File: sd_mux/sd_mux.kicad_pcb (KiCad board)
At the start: 2 copper layers, 86.4 x 54.6 mm, 22 parts, among them IC1 SN74CBT3257DR, IC2 SN74CBT3257DR, J1 MICRO SD CARD, J2 DEVICE 1, J3 DEVICE 2, J4 CONTROL

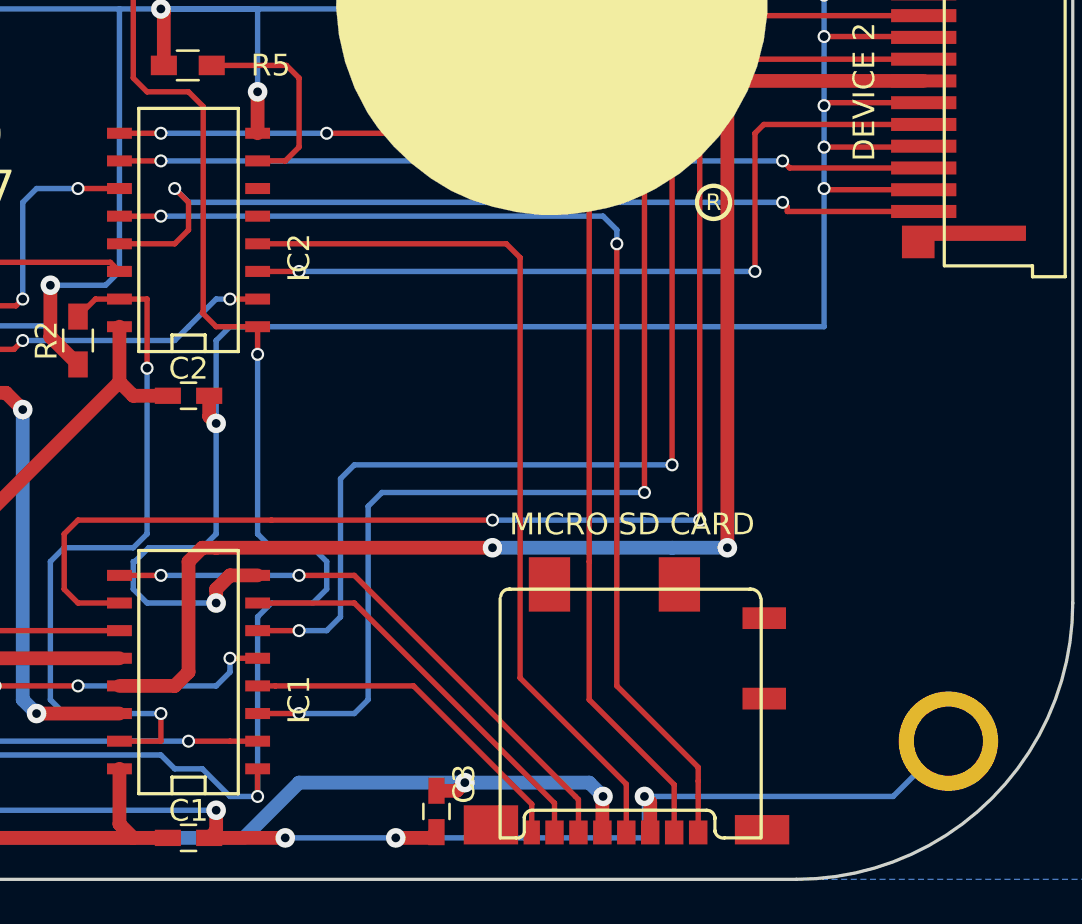
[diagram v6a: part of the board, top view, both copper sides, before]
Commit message: swapped SD card footprint
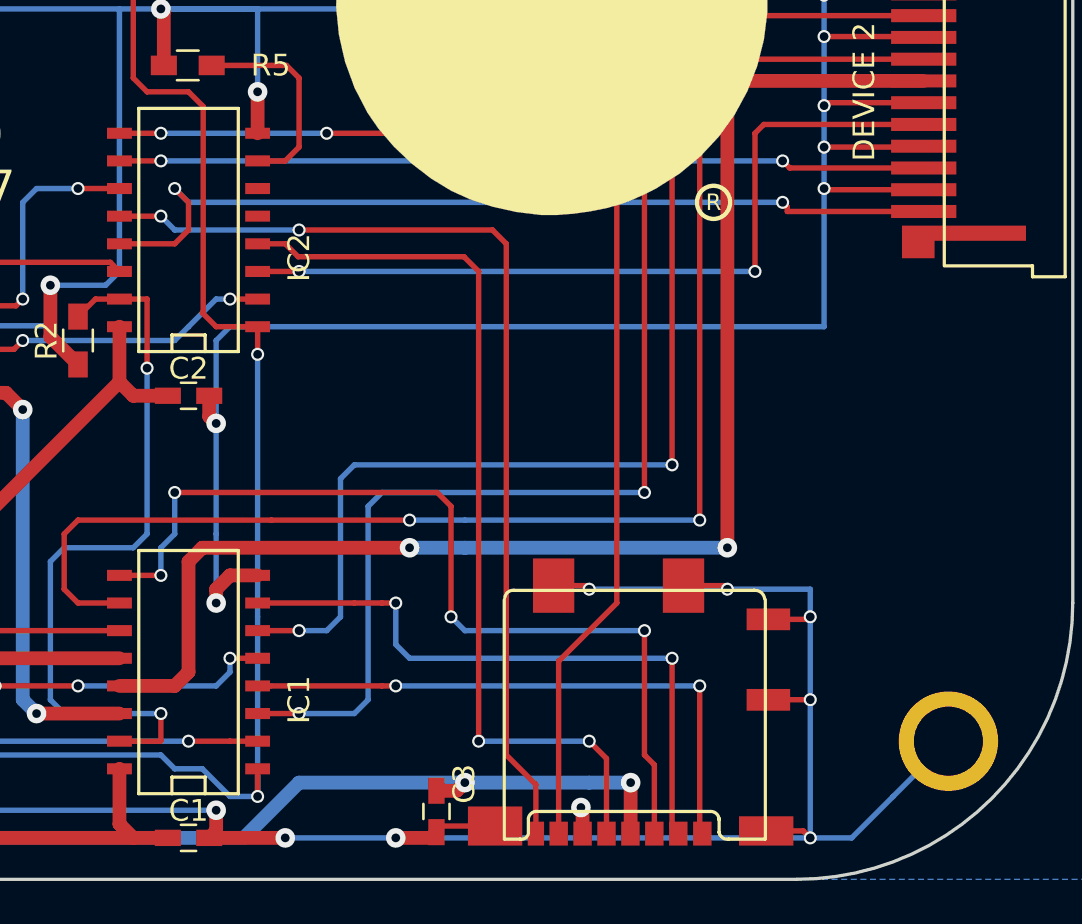
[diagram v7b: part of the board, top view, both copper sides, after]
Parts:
- J1: value MICRO SD CARD -> Micro_SD_Card_Det
- moved J1 0.20 mm to (167.8, 120.1)
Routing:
- net GND: track 364.7 -> 392.1 mm, vias 21 -> 26
- net Net-(IC1-Pad9): track 26.9 -> 42.7 mm, vias 2 -> 4
- net Net-(IC1-Pad4): track 16.2 -> 27.2 mm, vias 0 -> 2
- net Net-(IC1-Pad7): track 18.8 -> 29.4 mm, vias 0 -> 2
- net Net-(IC2-Pad12): track 52.4 -> 46.0 mm
- net device_select: track 107.7 -> 103.4 mm
- net Net-(C3-Pad1): track 50.7 -> 52.4 mm
- net Net-(IC2-Pad4): track 40.8 -> 41.9 mm, vias 0 -> 2
- net Net-(IC2-Pad9): track 55.0 -> 55.8 mm

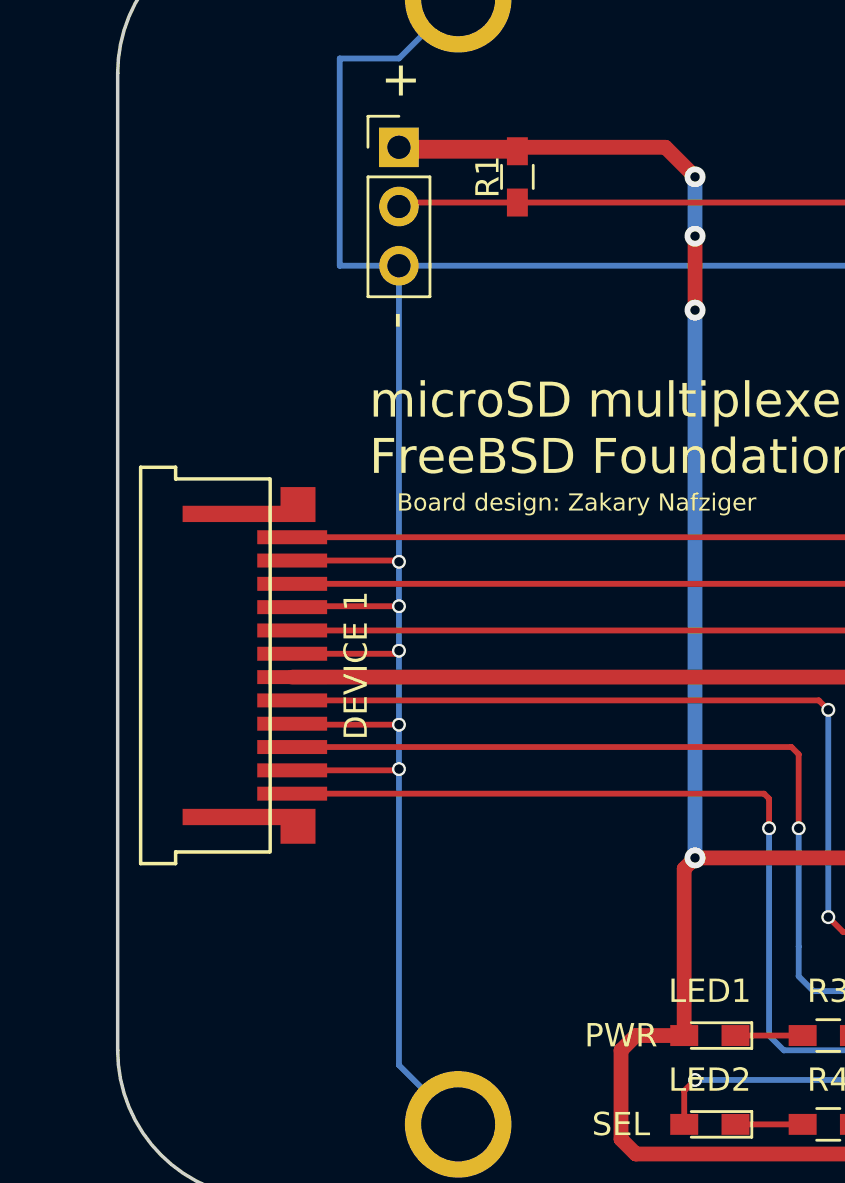
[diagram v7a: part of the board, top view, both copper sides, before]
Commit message: rerouted power line to avoid cut in ground plane
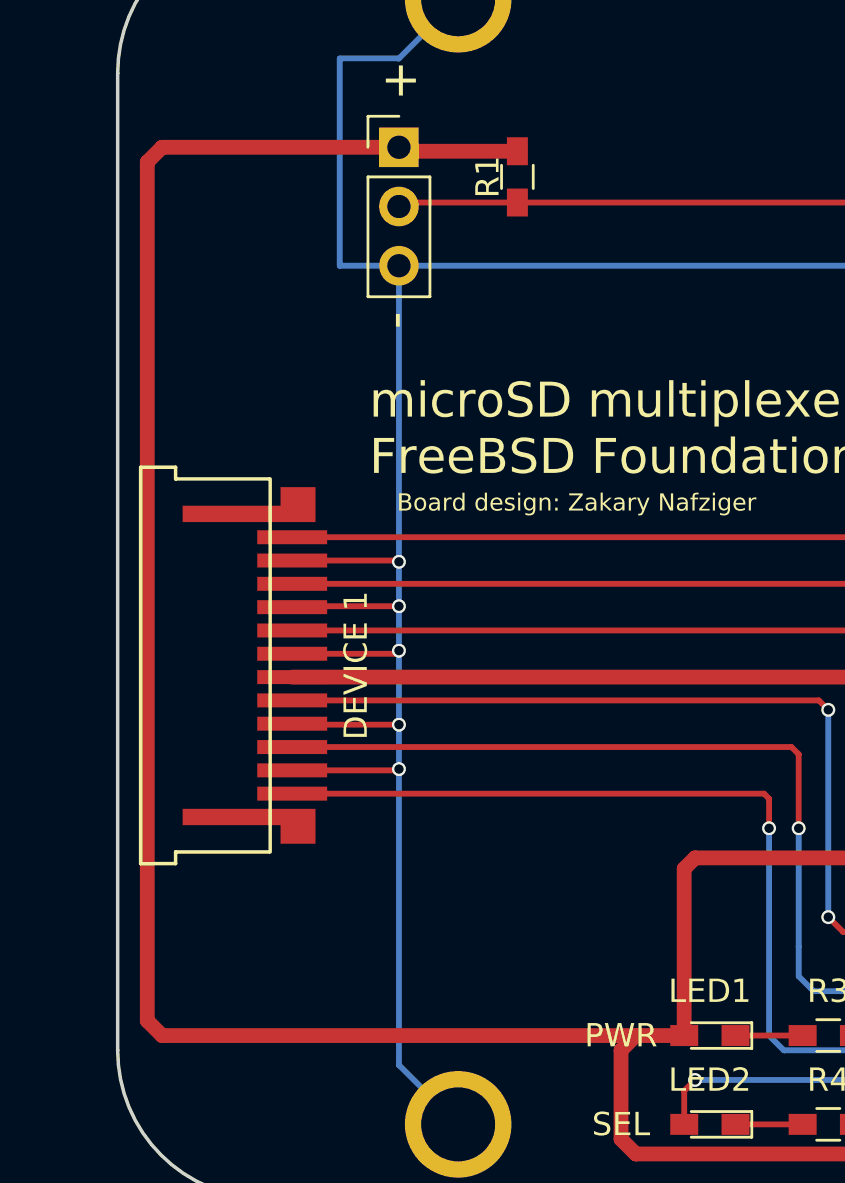
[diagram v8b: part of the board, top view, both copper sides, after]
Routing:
- net VCC: track 115.3 -> 142.0 mm, vias 4 -> 0
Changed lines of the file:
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@@
     (links 67)
     (no_connects 0)
-    (area 101.524999 67.234999 188.035001 121.995001)
+    (area 95.25 64.77 193.614049 122.87)
     (thickness 1.6)
     (drawings 16)
-    (tracks 431)
+    (tracks 427)
     (zones 0)
     (modules 22)
@@
   )
   (setup
-    (last_trace_width 0.25)
+    (last_trace_width 0.635)
     (user_trace_width 0.635)
     (user_trace_width 1.27)
@@
     (effects (font (size 1.5 1.5) (thickness 0.3)))
   )
-  (via (at 126.365 107.315) (size 0.9) (drill 0.4) (layers F.Cu B.Cu) (net 1))
-  (via (at 126.365 83.82) (size 0.9) (drill 0.4) (layers F.Cu B.Cu) (net 1))
-  (via (at 126.365 80.645) (size 0.9) (drill 0.4) (layers F.Cu B.Cu) (net 1))
-  (via (at 126.365 78.105) (size 0.9) (drill 0.4) (layers F.Cu B.Cu) (net 1))
+  (segment (start 123.825 114.935) (end 103.505 114.935) (width 0.635) (layer F.Cu) (net 1))
+  (segment (start 103.505 114.935) (end 102.87 114.3) (width 0.635) (layer F.Cu) (net 1))
+  (segment (start 102.87 114.3) (end 102.87 77.47) (width 0.635) (layer F.Cu) (net 1))
+  (segment (start 102.87 77.47) (end 103.505 76.835) (width 0.635) (layer F.Cu) (net 1))
+  (segment (start 103.505 76.835) (end 113.665 76.835) (width 0.635) (layer F.Cu) (net 1))
   (segment (start 135.89 107.315) (end 144.145 99.06) (width 0.635) (layer F.Cu) (net 1))
   (segment (start 126.365 107.315) (end 135.89 107.315) (width 0.635) (layer F.Cu) (net 1))
-  (segment (start 126.365 78.105) (end 125.095 76.835) (width 0.635) (layer F.Cu) (net 1))
-  (segment (start 125.095 76.835) (end 113.665 76.835) (width 0.635) (layer F.Cu) (net 1))
-  (segment (start 126.365 80.645) (end 126.365 78.105) (width 0.635) (layer B.Cu) (net 1))
-  (segment (start 126.365 83.82) (end 126.365 80.645) (width 0.635) (layer F.Cu) (net 1))
-  (segment (start 126.365 107.315) (end 126.365 83.82) (width 0.635) (layer B.Cu) (net 1))
   (segment (start 144.78 120.015) (end 123.825 120.015) (width 0.635) (layer F.Cu) (net 1))
   (segment (start 123.825 120.015) (end 123.19 119.38) (width 0.635) (layer F.Cu) (net 1))
